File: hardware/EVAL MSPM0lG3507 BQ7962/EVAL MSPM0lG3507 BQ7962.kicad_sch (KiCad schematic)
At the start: 126 parts, among them J1 Conn_01x09_Socket, J10 Screw_Terminal_01x02, J11 Screw_Terminal_01x02, J12 Screw_Terminal_01x02, J13 Screw_Terminal_01x02, J14 Screw_Terminal_01x02, J16 Conn_02x02_Odd_Even, J17 Conn_01x02_Pin, J18 Conn_01x02_Pin, J2 Conn_02x05_Odd_Even, J3 Conn_01x04_Pin, J4 Screw_Terminal_01x02, J5 Conn_01x03_Pin, J7 Screw_Terminal_01x02, J8 Screw_Terminal_01x02, J9 Screw_Terminal_01x02, SW1 SW_Push, SW2 SW_Push, SW3 SW_Push, U1 TPD6E004RSER, U2 MCU-MSM0G3507SPM, U3 TPD6E004RSER, U4 FCX495, U7 PBQ76952PFBT

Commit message: cleaned up schematics
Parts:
- removed C14, C34, C36, C42: 2.2u, Capacitor_THT:CP_Radial_D8.0mm_P2.50mm, symbol Device:C_Polarized_Small
- removed D3, D4: LED, LED_SMD:LED_0805_2012Metric_Pad1.15x1.40mm_HandSolder, symbol Device:LED
- removed D5: 100V, Diode_SMD:D_1206_3216Metric_Pad1.42x1.75mm_HandSolder, symbol Device:D_Schottky_Small
- added C14, C17: 10u, Capacitor_SMD:C_1206_3216Metric_Pad1.33x1.80mm_HandSolder, symbol Device:C_Small
- added C25: 1u, Capacitor_SMD:C_1812_4532Metric, symbol Device:C_Small
- added D1, D2: LED, LED_SMD:LED_0201_0603Metric_Pad0.64x0.40mm_HandSolder, symbol Device:LED
- added R24: 50k, Resistor_SMD:R_1206_3216Metric_Pad1.30x1.75mm_HandSolder, symbol Device:R_US
- added U8: FCX495, Package_TO_SOT_SMD:SOT-89-3, symbol zzLocalLibrary:FCX485_NPN_BJT
- R18: value 200 -> 5k
- R7: value 47k -> 50k; mouser (none) -> https://www.mouser.com/ProductDetail/YAGEO/RT1206BRD0750KL?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
- U4: mouser (none) -> https://www.mouser.com/ProductDetail/Diodes-Incorporated/FC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
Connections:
- net +3.3V: now also R16.2, R18.1, C14.1, D1.2 (A)
- net +5V: now also D2.2 (A)
- net +BATT: now also R24.2, U8.2
- net GND: now also C14.2, C17.2, C25.2; no longer R16.1
- net PA18: no longer J1.9 (Pin_9), U1.7 (IO6)
- net PA19_SWDIO: now also R16.1
- net PA20_SWCLK: now also R18.2
- net at R15.1, U7.25 (ALERT): no longer R16.2
- net at C26.1, C39.1, C40.1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: now also U8.3; no longer C28.1
- net at R11.2: now also U4.2, C25.1; no longer R18.1
- net at R1.1: now also D2.1 (K)
- net at TP11.1, U7.24 (REG18): now also C17.1
- net at R6.2: now also D1.1 (K)
- new net: C28.1, R24.1, U8.1
- new net XDS_BLS_INVOKE: U1.7 (IO6)
- no-connect marks 54 -> 56
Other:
- added sheet UART_USB (UART_USB.kicad_sch)
- note removed: "pull up done in software"
- moved on the sheet: C1, C28, R11, R15

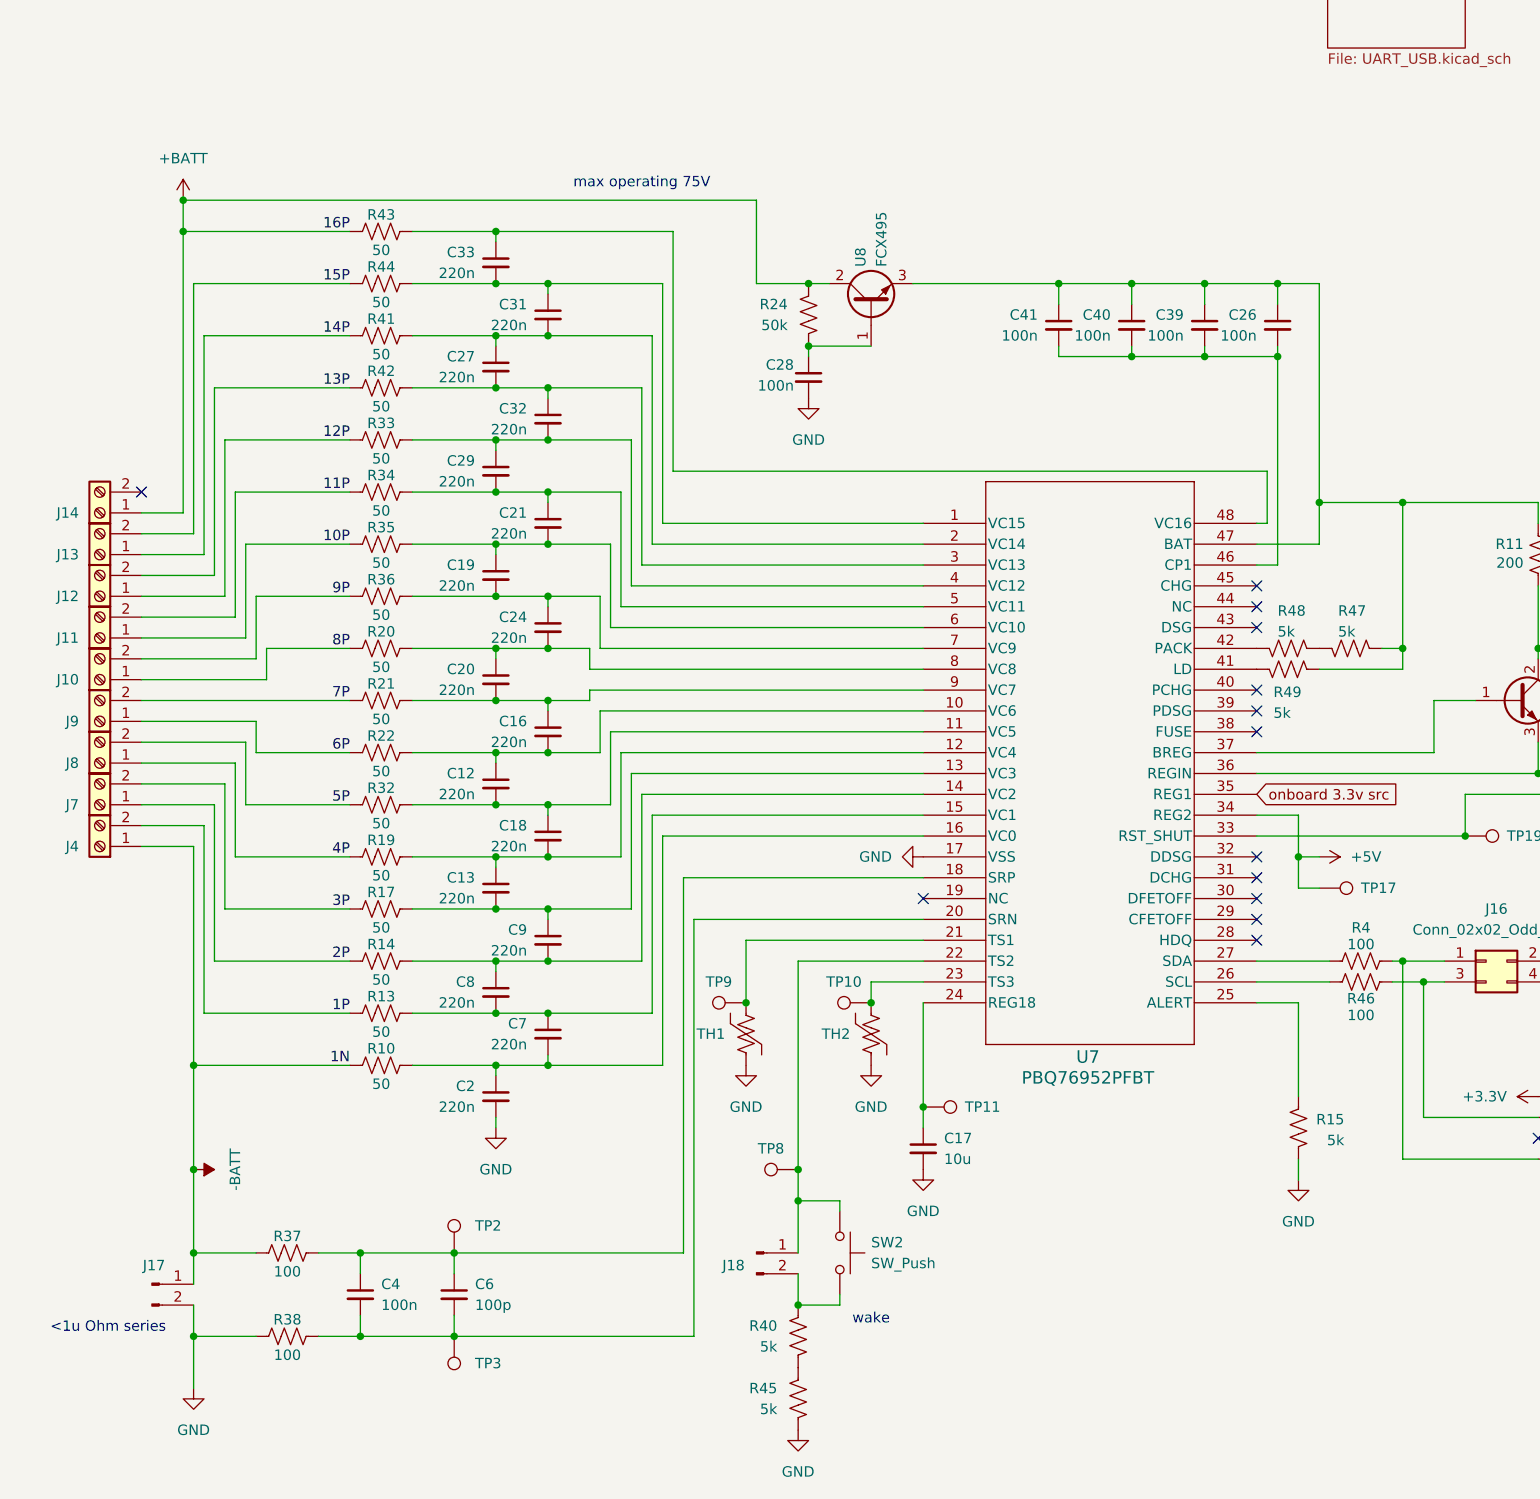
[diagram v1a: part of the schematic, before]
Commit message: made a hierarchical sheet for the BQ chip
Co-Authored-By: George Boone <yongboone1@gmail.com>
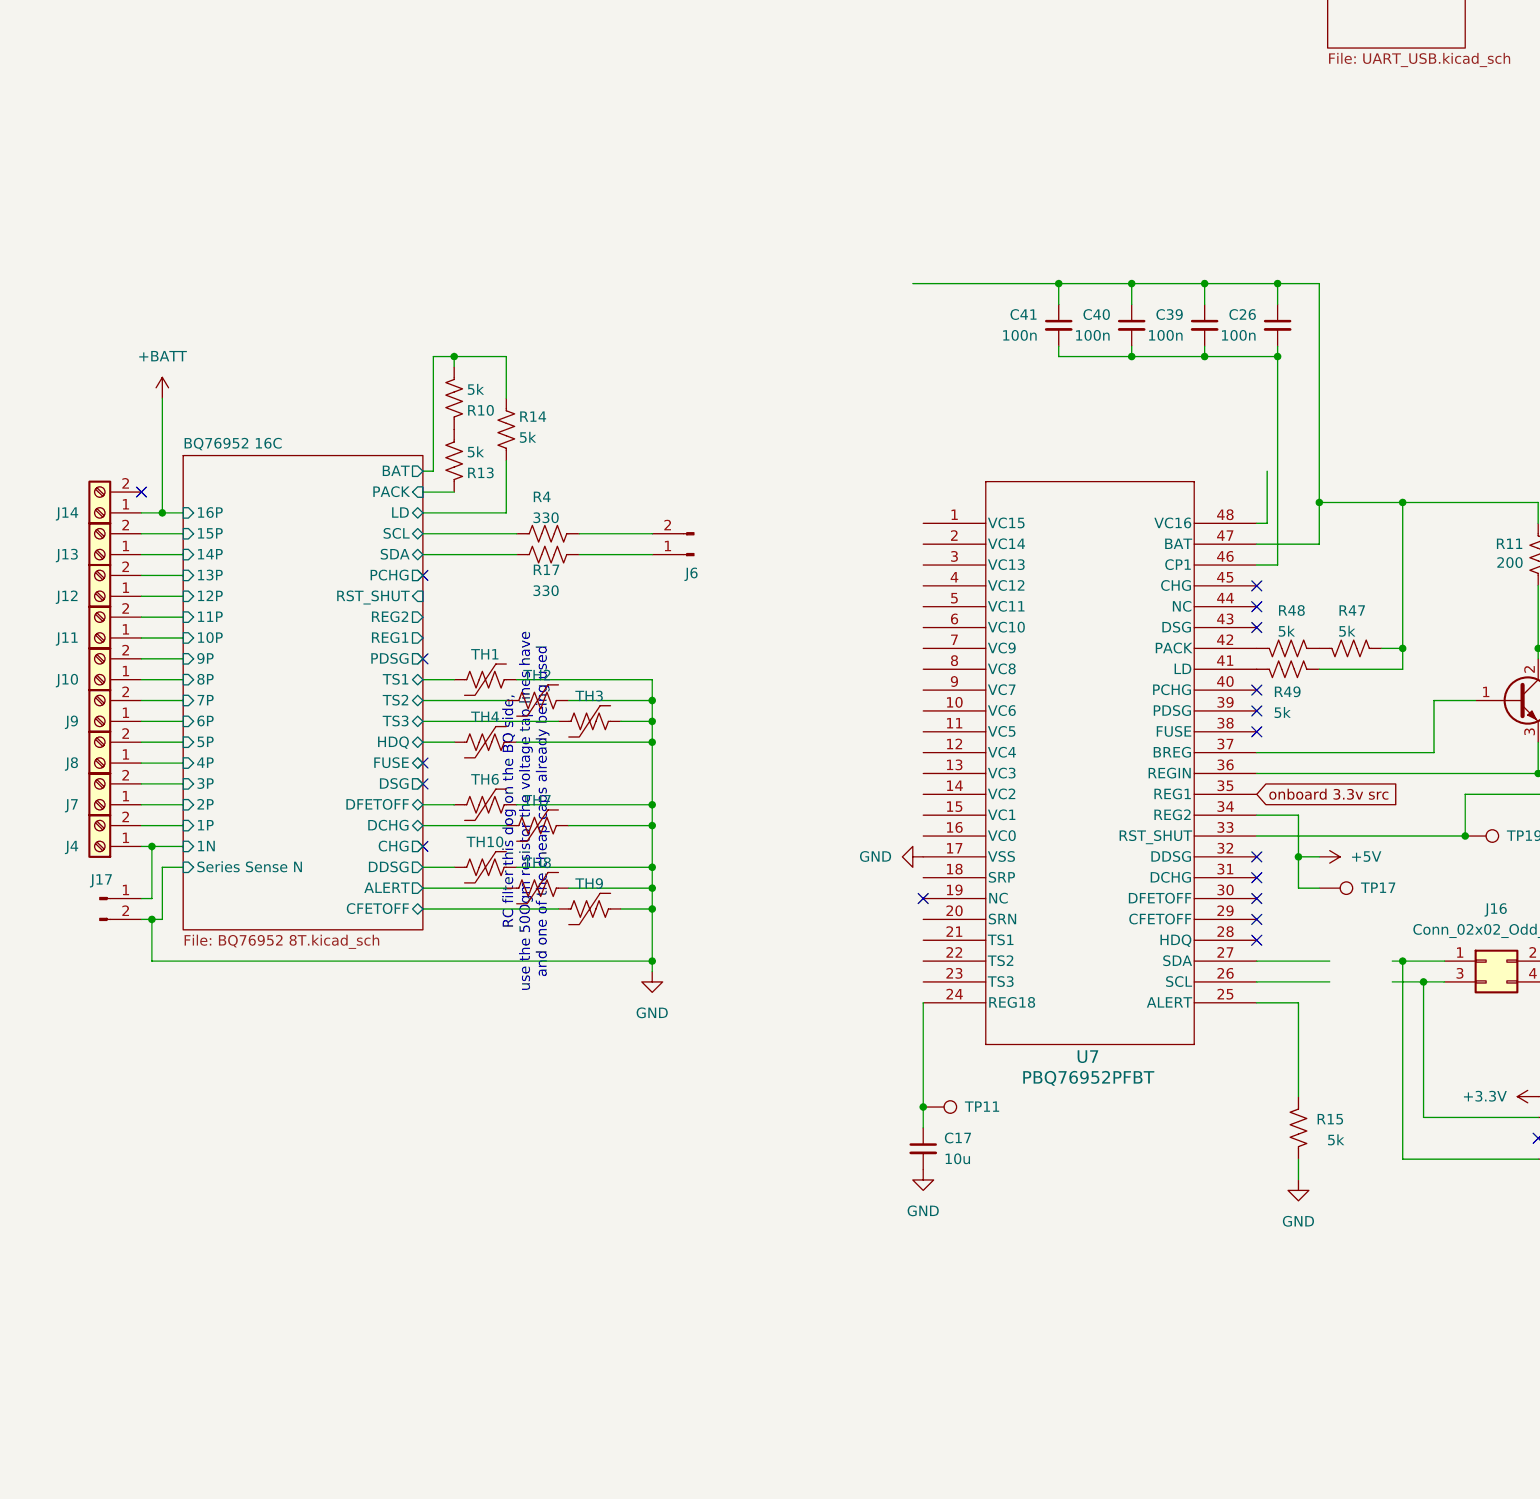
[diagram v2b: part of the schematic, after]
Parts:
- removed C12, C13, C16, C18, C19, C2, C20, C21, C24, C27, C29, C31, C32, C33, C7, C8, C9: 220n, Capacitor_SMD:C_1206_3216Metric_Pad1.33x1.80mm_HandSolder, symbol Device:C_Small
- removed C28, C4: 100n, Capacitor_SMD:C_1206_3216Metric_Pad1.33x1.80mm_HandSolder, symbol Device:C_Small
- removed C6: 100p, Capacitor_SMD:C_1206_3216Metric_Pad1.33x1.80mm_HandSolder, symbol Device:C_Small
- removed J18: Conn_01x02_Pin, Connector_PinHeader_2.54mm:PinHeader_1x02_P2.54mm_Vertical, symbol Connector:Conn_01x02_Pin
- removed R19, R20, R21, R22, R32, R33, R34, R35, R36, R41, R42, R43, R44: 50, Resistor_SMD:R_1206_3216Metric_Pad1.30x1.75mm_HandSolder, symbol Device:R_US
- removed R24: 50k, Resistor_SMD:R_1206_3216Metric_Pad1.30x1.75mm_HandSolder, symbol Device:R_US
- removed R37, R38, R46: 100, Resistor_SMD:R_1206_3216Metric_Pad1.30x1.75mm_HandSolder, symbol Device:R_US
- removed R40, R45: 5k, Resistor_SMD:R_1206_3216Metric_Pad1.30x1.75mm_HandSolder, symbol Device:R_US
- removed SW2: SW_Push, Button_Switch_SMD:SW_SPST_PTS645, symbol Switch:SW_Push
- removed TP10, TP2, TP3, TP8, TP9: TestPoint, TestPoint:TestPoint_Loop_D2.50mm_Drill1.0mm_LowProfile, symbol Connector:TestPoint
- removed U8: FCX495, Package_TO_SOT_SMD:SOT-89-3, symbol zzLocalLibrary:FCX485_NPN_BJT
- added J6: Conn_01x02_Pin, Connector_PinHeader_2.54mm:PinHeader_1x02_P2.54mm_Vertical, symbol Connector:Conn_01x02_Pin
- added TH10, TH3, TH4, TH6, TH7, TH8, TH9: Thermistor_US, Resistor_SMD:R_1206_3216Metric_Pad1.30x1.75mm_HandSolder, symbol Device:Thermistor_US
- C14: specs (none) -> 0.22uF, 50VDC, 10%, X7R, -55C, +125C
- R10, R13, R14: value 50 -> 5k
- R17: value 50 -> 330; mouser (none) -> https://www.mouser.com/ProductDetail/TE-Connectivity-Holswo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; specs (none) -> 250mW, 1%, 100PPM, 200V
- R4: value 100 -> 330; mouser (none) -> https://www.mouser.com/ProductDetail/TE-Connectivity-Holswo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; specs (none) -> 250mW, 1%, 100PPM, 200V
- TH1, TH2: mouser (none) -> https://www.mouser.com/ProductDetail/KYOCERA-AVX/NC20K00103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; specs (none) -> 3630kB, 10kOhms, 10%, -55C, +150C, 240mW
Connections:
- net GND: now also TH1.2, TH2.2, TH10.2, TH3.2, TH4.2, TH6.2, TH7.2, TH8.2, TH9.2; no longer TH1.1, TH2.1
- net at U7.21 (TS1): no longer TH1.2
- net at U7.23 (TS3): no longer TH2.2
- net at J16.1 (Pin_1), U3.5 (IO4): no longer R4.2
- net at U7.13 (VC3): no longer R17.2
- net at R13.2: now also R10.1; no longer U7.15 (VC1)
- net at U7.14 (VC2): no longer R14.2
- net at U7.16 (VC0): no longer R10.2
- net at U7.27 (SDA): no longer R4.1
- net -BATT renamed BQ76952 16C/1N
- net BQ76952 16C/1N: no longer R10.1
- net 10P renamed BQ76952 16C/10P
- net 11P renamed BQ76952 16C/11P
- net 12P renamed BQ76952 16C/12P
- net 13P renamed BQ76952 16C/13P
- net 14P renamed BQ76952 16C/14P
- net 15P renamed BQ76952 16C/15P
- net 1P renamed BQ76952 16C/1P
- net BQ76952 16C/1P: no longer R13.1
- net 2P renamed BQ76952 16C/2P
- net BQ76952 16C/2P: no longer R14.1
- net 3P: no longer names the net of R17.1
- net 3P: now also J6.1 (Pin_1); no longer J7.2 (Pin_2)
- net 4P renamed BQ76952 16C/4P
- net 5P renamed BQ76952 16C/5P
- net 6P renamed BQ76952 16C/6P
- net 7P renamed BQ76952 16C/7P
- net 8P renamed BQ76952 16C/8P
- net 9P renamed BQ76952 16C/9P
- new net: J6.2 (Pin_2), R4.2
- new net BQ76952 16C/3P: J7.2 (Pin_2)
- new net BQ76952 16C/ALERT: TH8.1
- new net BQ76952 16C/BAT: R10.2, R14.1
- new net BQ76952 16C/CFETOFF: TH9.1
- new net BQ76952 16C/DCHG: TH7.1
- new net BQ76952 16C/DDSG: TH10.1
- new net BQ76952 16C/DFETOFF: TH6.1
- new net BQ76952 16C/HDQ: TH4.1
- new net BQ76952 16C/LD: R14.2
- new net BQ76952 16C/PACK: R13.1
- new net BQ76952 16C/SCL: R4.1
- new net BQ76952 16C/SDA: R17.2
- new net BQ76952 16C/TS1: TH1.1
- new net BQ76952 16C/TS2: TH2.1
- new net BQ76952 16C/TS3: TH3.1
- no-connect marks 56 -> 61
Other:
- added sheet BQ76952 16C (BQ76952 8T.kicad_sch)
- note added: "RC filter this dog on the BQ side, use the 50Ogm resistor the voltage tap lines have and one of the cheap caps already being used"
- note removed: "<1u Ohm series"
- note removed: "max operating 75V"
- note removed: "wake"
- moved on the sheet: J17

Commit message: kjcaejjacljace
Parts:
- removed C1, C26, C39, C40, C41: 100n, Capacitor_SMD:C_1206_3216Metric_Pad1.33x1.80mm_HandSolder, symbol Device:C_Small
- removed C17: 10u, Capacitor_SMD:C_1206_3216Metric_Pad1.33x1.80mm_HandSolder, symbol Device:C_Small
- removed C25: 1u, Capacitor_SMD:C_1812_4532Metric, symbol Device:C_Small
- removed J16: Conn_02x02_Odd_Even, Connector_PinHeader_2.54mm:PinHeader_2x02_P2.54mm_Vertical, symbol Connector_Generic:Conn_02x02_Odd_Even
- removed R47, R48, R49: 5k, Resistor_SMD:R_1206_3216Metric_Pad1.30x1.75mm_HandSolder, symbol Device:R_US
- removed SW3: SW_Push, Button_Switch_SMD:SW_SPST_PTS645, symbol Switch:SW_Push
- removed TH10: Thermistor_US, Resistor_SMD:R_1206_3216Metric_Pad1.30x1.75mm_HandSolder, symbol Device:Thermistor_US
- removed TP19, TP20: TestPoint, TestPoint:TestPoint_Loop_D2.50mm_Drill1.0mm_LowProfile, symbol Connector:TestPoint
- removed U1, U3: TPD6E004RSER, zzLocalLibraries-Footprints:RSE8, symbol zzLocalLibrary:TPD6E004RSER
- removed U4: FCX495, Package_TO_SOT_SMD:SOT-89-3, symbol zzLocalLibrary:FCX485_NPN_BJT
- removed U7: PBQ76952PFBT, zzLocalLibraries-Footprints:BQ76952_PFB48_TEX, symbol zzLocalLibrary:PBQ76952PFBT
- added J15: Conn_01x02_Pin, Connector_PinHeader_2.54mm:PinHeader_1x02_P2.54mm_Vertical, symbol Connector:Conn_01x02_Pin
- added Q1: ~, zzLocalLibraries-Footprints:SOT8001, symbol zzLocalLibrary:NX138BKHH
- added R46: 5k, Resistor_SMD:R_1206_3216Metric_Pad1.30x1.75mm_HandSolder, symbol Device:R_US
- added TH5: Thermistor_US, Resistor_SMD:R_1206_3216Metric_Pad1.30x1.75mm_HandSolder, symbol Device:Thermistor_US
- added TP10, TP13, TP3: TestPoint, TestPoint:TestPoint_Loop_D2.50mm_Drill1.0mm_LowProfile, symbol Connector:TestPoint
- added TP9: TestPoint, TestPoint:TestPoint_THTPad_3.0x3.0mm_Drill1.5mm, symbol Connector:TestPoint
- C11, C5: mouser (none) -> https://www.mouser.com/ProductDetail/Samsung-Electro-Mechan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; specs (none) -> 50VDC, X7R, 10%, -55C, +125C, 220nF; unit x10 (none) -> 0.05
- C14: specs 0.22uF, 50VDC, 10%, X7R, -55C, +125C -> 10uF, 50VDC, X5R, 10%, -55C, +85C; unit x10 (none) -> 0.07
- D1, D2: specs (none) -> amber, 5mA, 1.9V, 75mW, -40C, +85C; unit x10 (none) -> 0.12
- D6: mouser (none) -> https://www.mouser.com/ProductDetail/Bivar/SM0603GCL?qs=sGA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; specs (none) -> green, 2mA, 1.9V, 78mW, -30C, +80C; unit x10 (none) -> 0.42
- R1: mouser (none) -> https://www.mouser.com/ProductDetail/Panasonic/ERJ-P08J201V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; specs (none) -> 200Ohms, 660mW, 200PPM, 500V, 5%, -55C, +155C
- R11: value 200 -> 50k; mouser (none) -> https://www.mouser.com/ProductDetail/YAGEO/RT1206BRD0750KL?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
- R17, R4: value 330 -> 150; mouser https://www.mouser.com/ProductDetail/TE-Connectivity-Holswo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 -> https://www.mouser.com/ProductDetail/YAGEO/AC1206FR-7W150RL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; specs 250mW, 1%, 100PPM, 200V -> 150Ohm, 500mW, 1%, 200V, -55C, +155C
- R2: value 5k -> 50k; mouser (none) -> https://www.mouser.com/ProductDetail/YAGEO/RT1206BRD0750KL?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
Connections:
- net +5V: no longer TP17.1
- net BQ76952 16C/DCHG: now also TH6.1; no longer TH7.1
- net BQ76952 16C/DDSG: now also TH7.1
- net BQ76952 16C/DFETOFF: now also TH5.1; no longer TH6.1
- net BQ76952 16C/RST_SHUT: now also R11.2, Q1.2 (S)
- net GND: now also R11.1, TH5.2, TP9.1; no longer R15.2
- net PA15_I2C1_SCL: now also J15.1 (Pin_1), TP13.1
- net PA16_I2C1_SDA: now also TP17.1, J15.2 (Pin_2)
- net PB26: now also R2.2, Q1.1 (G)
- net at J6.2 (Pin_2), R4.2: now also R15.1, TP10.1
- net at C11.1, C5.1, U2.32 (VCORE): now also TP3.1
- net at TP11.1: now also J6.1 (Pin_1), R17.1, R46.1
- net BQ76952 16C/1N renamed -BATT
- new net BQ0_3.3v: Q1.3 (D), R15.2, R46.2
- no-connect marks 61 -> 45
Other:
- note added: "2"
- note added: "BLS invoke pin (boot strap loader). well use this later down the line"
- note added: "EVAL MSPM0G3507 BQ76952"
- note added: "Files found at github.com/Gregification/BeeMS"
- note added: "ex large"
- note removed: "RC filter this dog on the BQ side, use the 50Ogm resistor the voltage tap lines have and one of the cheap caps already being used"
- note removed: "XDS supply (if present) overrides onboard supply. RC delay for programming timing"
- note removed: "edge conn"
- note removed: "port vaporizer 5000"
- note removed: "reset"
- moved on the sheet: J17, J6, TH6, TH7, TP14, TP15, TP16

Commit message: mouser doom scrolling labor
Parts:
- removed R15, R46: 5k, Resistor_SMD:R_1206_3216Metric_Pad1.30x1.75mm_HandSolder, symbol Device:R_US
- added C17, C19: 10u, Capacitor_SMD:C_1206_3216Metric_Pad1.33x1.80mm_HandSolder, symbol Device:C_Small
- added C18: 100p, Capacitor_SMD:C_1206_3216Metric_Pad1.33x1.80mm_HandSolder, symbol Device:C_Small
- added L2: 1u, Inductor_SMD:L_0805_2012Metric_Pad1.15x1.40mm_HandSolder, symbol Device:L_Small
- added R47, R48, R56, R57, R58: 100k, Resistor_SMD:R_1206_3216Metric_Pad1.30x1.75mm_HandSolder, symbol Device:R_US
- added U3: TPS62A02ADRL, Package_TO_SOT_SMD:SOT-563, symbol Regulator_Switching:TPS62A02ADRL
- C15, C3: mouser (none) -> https://www.mouser.com/ProductDetail/Walsin/1206B104K251CT?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; specs (none) -> 100nF, 250VDC, X7R, 10%, -55C, +125C; unit x10 (none) -> 0.062
- R10, R13, R14, R16, R18, R5, R9: value 5k -> 4.99k; mouser (none) -> https://www.mouser.com/ProductDetail/SEI-Stackpole/RNCP1206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; specs (none) -> 4.99kOhm, 200V, 500mW, 1%, 100PPM, -55C, +155C
- R11, R2, R7: value 50k -> 49.9k; mouser https://www.mouser.com/ProductDetail/YAGEO/RT1206BRD0750KL?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 -> https://www.mouser.com/ProductDetail/SEI-Stackpole/RNCP1206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; specs (none) -> 49.9kOhms, 500mW, 1%, 200V, 100PPM, -55C, +155C; unit x10 (none) -> 0.014
- R8: mouser (none) -> https://www.mouser.com/ProductDetail/Bourns/CHV1206-FX-1003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; specs (none) -> 100kOhm, 800V, 250mW, 100PPM, 1%, -55C, 155C; unit x10 (none) -> 0.083
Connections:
- net PA8_UART0-RTS: now reaches U2.54 (PA8)
- net PA9_UART0-CTS: now reaches U2.55 (PA9)
- new net: R47.1, U3.6 (PG)
- new net: R47.2, R48.1
- new net: C17.1, R48.2, U3.3 (VIN), U3.4 (EN)
- new net: C17.2, R58.1, U3.1 (GND)
- new net: L2.1, U3.2 (SW)
- new net: C18.2, C19.2, R57.1, R58.2, U3.5 (FB)
- new net: R56.1, R57.2
- new net: C18.1, C19.1, L2.2, R56.2
- no-connect marks 45 -> 43
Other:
- sheet UART_USB ports: added CTS, RTS, RXD, TXD, VDD, VSS; removed none
- moved on the sheet: J15, J6, TP10, TP11, TP13, TP17
